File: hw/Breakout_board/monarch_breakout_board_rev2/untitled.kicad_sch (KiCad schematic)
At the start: 12 parts, among them J1 5037630491, J2 5037630491, J3 5037630491, J4 Conn_01x02

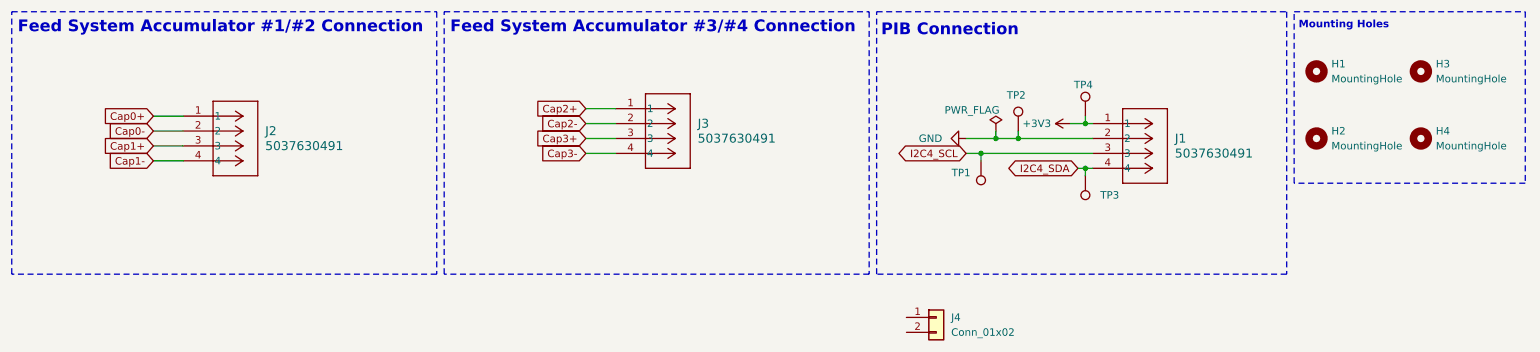
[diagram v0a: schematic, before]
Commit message: ADXL355 Schematic Addition + I2C Problem within the chip
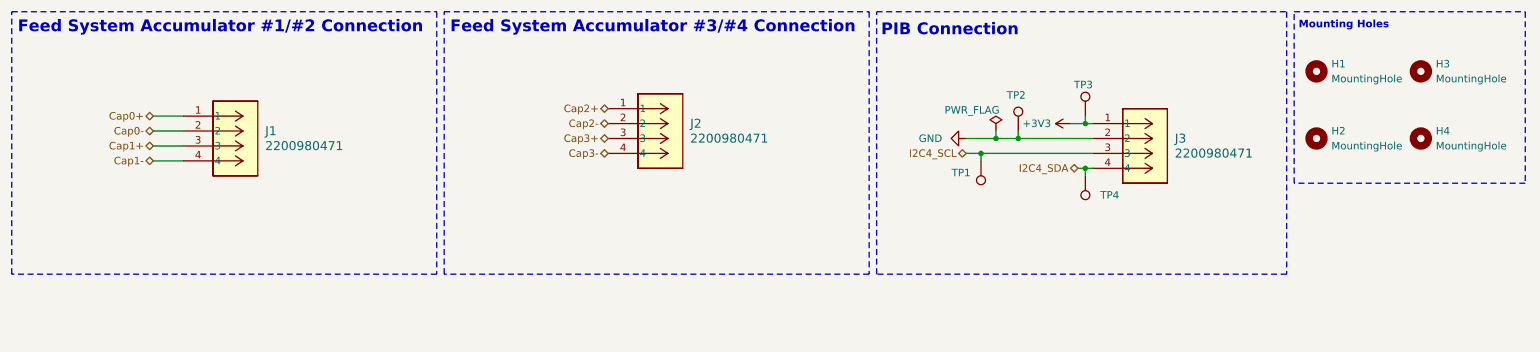
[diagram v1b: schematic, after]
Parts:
- removed J1, J2, J3: 5037630491, Connector 4 Pin:CONN_5037630000-SD_04_MOL, symbol Connectors 4 Pin:5037630491
- removed J4: Conn_01x02, symbol Connector_Generic:Conn_01x02
- added J1, J2, J3: 2200980471, Connector_Molex_Micro-Lock-Plus:Molex_Micro-Lock_2200980471_1x04_P1.25mm_Horizontal, symbol 5037630491:5037630491
- renumbered TP4 to TP3, TP3 to TP4
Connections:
- net +3V3: now also J3.1
- net Cap0+: now also J1.1
- net Cap0-: now also J1.2
- net Cap1+: now also J1.3
- net Cap1-: now also J1.4
- net Cap2+: now also J2.1
- net Cap2-: now also J2.2
- net Cap3+: now also J2.3
- net Cap3-: now also J2.4
- net GND: now also J3.2
- net I2C4_SCL: now also J3.3
- net I2C4_SDA: now also J3.4
